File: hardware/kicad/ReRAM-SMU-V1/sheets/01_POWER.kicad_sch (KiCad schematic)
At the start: 1 part

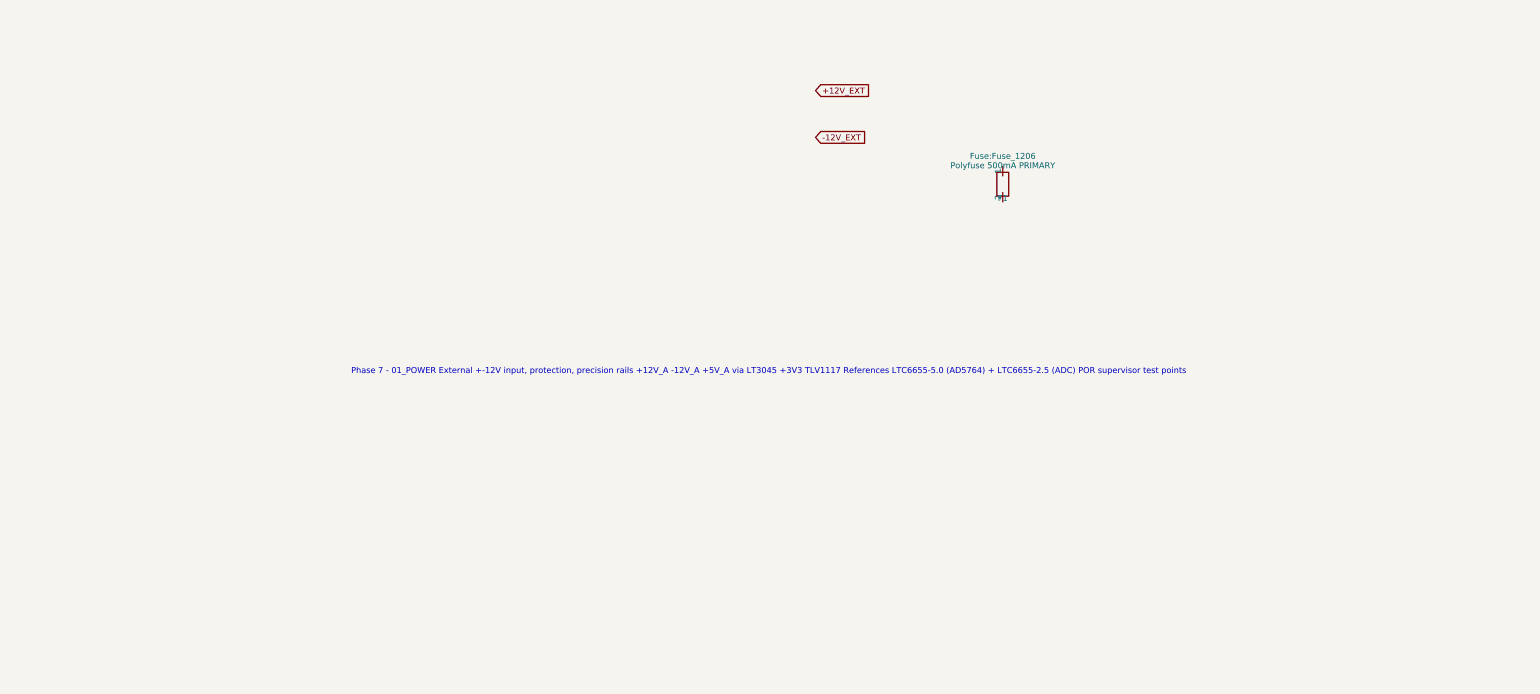
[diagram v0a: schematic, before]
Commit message: hardware: pre-ERC manufacturer corrections (LT1970 physical pins, ADS1262 TSSOP-28, MCU G431RBT6, 74LVC1G74 latch, LT5400 Kelvin, AD5764 rails, ADS1262 bipolar)
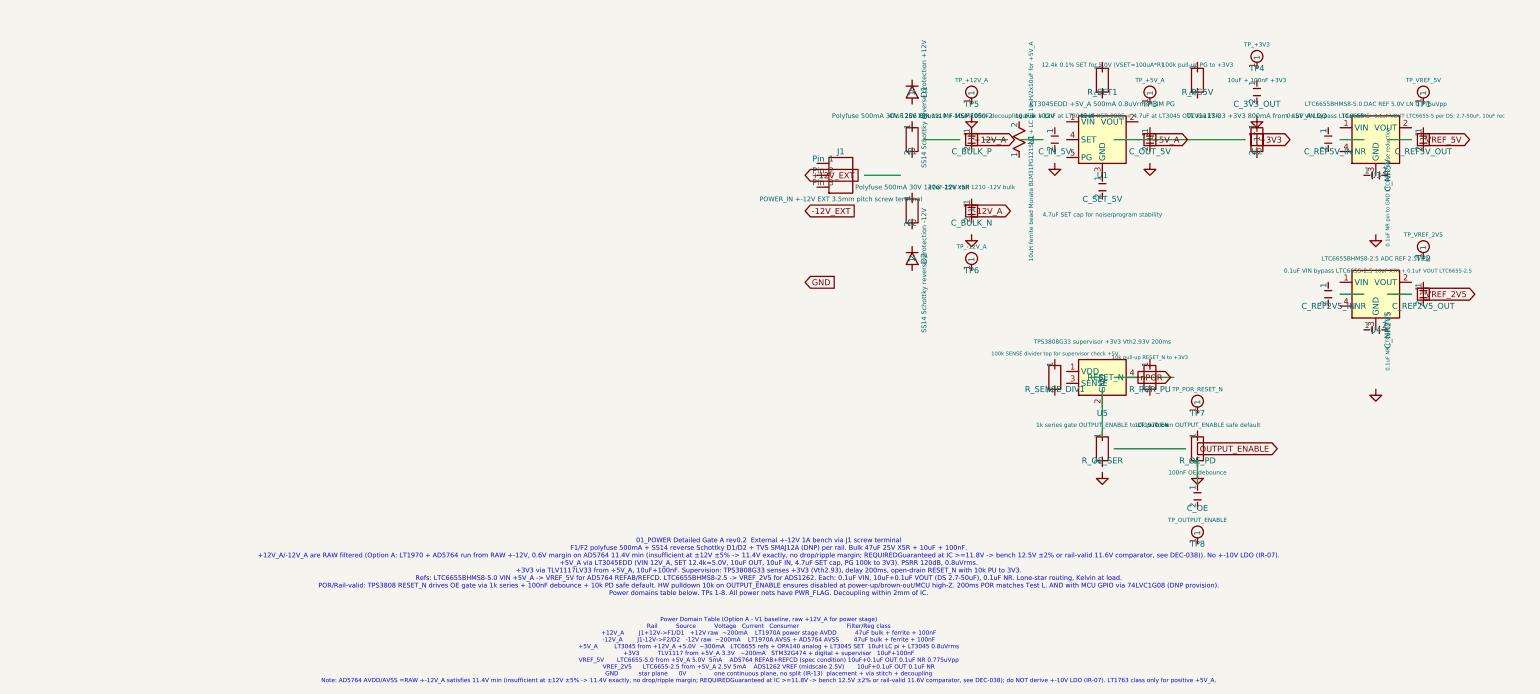
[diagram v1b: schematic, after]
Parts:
- added C_3V3_OUT: 10uF + 100nF +3V3, Capacitor_SMD:C_0805_2012Metric, symbol Device:C
- added C_BULK_N: 47uF 25V X5R 1210 -12V bulk, Capacitor_SMD:C_1210_3225Metric, symbol Device:C
- added C_BULK_P: 47uF 25V X5R 1210 + 10uF 100nF decoupling bulk +1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, Capacitor_SMD:C_1210_3225Metric, symbol Device:C
- added C_IN_5V: 10uF + 100nF at LT3045 IN, Capacitor_SMD:C_0805_2012Metric, symbol Device:C
- added C_NR2V5: 0.1uF NR LTC6655-2.5, Capacitor_SMD:C_0603_1608Metric, symbol Device:C
- added C_NR5V: 0.1uF NR pin to GND LTC6655 noise reduction, Capacitor_SMD:C_0603_1608Metric, symbol Device:C
- added C_OE: 100nF OE debounce, Capacitor_SMD:C_0603_1608Metric, symbol Device:C
- added C_OUT_5V: 10uF X5R 0805 + 4.7uF at LT3045 OUT low ESR, Capacitor_SMD:C_0805_2012Metric, symbol Device:C
- added C_REF2V5_IN: 0.1uF VIN bypass LTC6655-2.5, Capacitor_SMD:C_0603_1608Metric, symbol Device:C
- added C_REF2V5_OUT: 10uF X7R + 0.1uF VOUT LTC6655-2.5, Capacitor_SMD:C_0805_2012Metric, symbol Device:C
- added C_REF5V_IN: 0.1uF VIN bypass LTC6655-5, Capacitor_SMD:C_0603_1608Metric, symbol Device:C
- added C_REF5V_OUT: 10uF X7R + 0.1uF VOUT LTC6655-5 per DS: 2.7-50uF,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, Capacitor_SMD:C_0805_2012Metric, symbol Device:C
- added C_SET_5V: 4.7uF SET cap for noise/program stability, Capacitor_SMD:C_0603_1608Metric, symbol Device:C
- added D1: SS14 Schottky reverse protection +12V, Diode_SMD:D_SMA, symbol Device:D_Schottky
- added D2: SS14 Schottky reverse protection -12V, Diode_SMD:D_SMA, symbol Device:D_Schottky
- added F2: Polyfuse 500mA 30V 1206 -12V rail, Fuse:Fuse_1206_3216Metric, symbol Device:R
- added J1: POWER_IN +-12V EXT 3.5mm pitch screw terminal, Connector_Screw:Connector_Screw_Terminal_3.5mm_3pin, symbol Connector_Generic:Conn_03x01_Odd_Even
- added L1: 10uH ferrite bead Murata BLM31PG121SN1 + LC pi 10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, Inductor_SMD:L_1206_3216Metric, symbol Device:L
- added R_OE_PD: 10k pulldown OUTPUT_ENABLE safe default, Resistor_SMD:R_0603_1608Metric, symbol Device:R
- added R_OE_SER: 1k series gate OUTPUT_ENABLE to LT1970 EN, Resistor_SMD:R_0603_1608Metric, symbol Device:R
- added R_PG5V: 100k pull-up PG to +3V3, Resistor_SMD:R_0603_1608Metric, symbol Device:R
- added R_POR_PU: 10k pull-up RESET_N to +3V3, Resistor_SMD:R_0603_1608Metric, symbol Device:R
- added R_SENSE_DIV1: 100k SENSE divider top for supervisor check +5V, Resistor_SMD:R_0603_1608Metric, symbol Device:R
- added R_SET1: 12.4k 0.1% SET for 5.0V (VSET=100uA*R), Resistor_SMD:R_0603_1608Metric, symbol Device:R
- added TP1: TP_VREF_5V, symbol ReRAM_SMU:TestPoint
- added TP2: TP_VREF_2V5, symbol ReRAM_SMU:TestPoint
- added TP3: TP_+5V_A, symbol ReRAM_SMU:TestPoint
- added TP4: TP_+3V3, symbol ReRAM_SMU:TestPoint
- added TP5: TP_+12V_A, symbol ReRAM_SMU:TestPoint
- added TP6: TP_-12V_A, symbol ReRAM_SMU:TestPoint
- added TP7: TP_POR_RESET_N, symbol ReRAM_SMU:TestPoint
- added TP8: TP_OUTPUT_ENABLE, symbol ReRAM_SMU:TestPoint
- added U1: LT3045EDD +5V_A 500mA 0.8uVrms ILIM PG, Package_DFN:DFN-12_3x3mm_P0.45mm_EP, symbol ReRAM_SMU:LT3045
- added U2: TLV1117-33 +3V3 800mA from +5V_A LDO, Package_TO_SOT_SMD:SOT-223-3_TabPin2, symbol Device:R
- added U3: LTC6655BHMS8-5.0 DAC REF 5.0V LN 0.775uVpp, Package_SO:MSOP-8_3x3mm_P0.65mm, symbol ReRAM_SMU:LTC6655-5
- added U4: LTC6655BHMS8-2.5 ADC REF 2.5V LN, Package_SO:MSOP-8_3x3mm_P0.65mm, symbol ReRAM_SMU:LTC6655-2V5
- added U5: TPS3808G33 supervisor +3V3 Vth2.93V 200ms, Package_TO_SOT_SMD:SOT-23-6, symbol ReRAM_SMU:TPS3808
- F1: value Polyfuse 500mA PRIMARY -> Polyfuse 500mA 30V 1206 Bourns MF-MSMF050-2; footprint Fuse:Fuse_1206 -> Fuse:Fuse_1206_3216Metric
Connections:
- new net: C_SET_5V.1, U1.3 (GND)
- new net nPOR: U5.4 (RESET_N)
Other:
- note added: "01_POWER Detailed Gate A rev0.2 External +-12V 1A bench via J1 screw terminal F1/F2 polyfuse 500mA + SS14 reverse Schottky D1/D2 + TVS SMAJ12A (DNP) per rail. Bulk 47uF 25V X5R + 10uF + 100nF. +12V_A/-12V_A are RAW filtered (Option A: LT1970 + AD5764 run from RAW +-12V, 0.6V margin on AD5764 11.4V min (insufficient at ±12V ±5% -> 11.4V exactly, no drop/ripple margin; REQUIREDGuaranteed at IC >=11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"
- note added: "Power Domain Table (Option A - V1 baseline, raw +12V_A for power stage) Rail Source Voltage Current Consumer Filter/Reg class +12V_A J1+12V->F1/D1 +12V raw ~200mA LT1970A power stage AVDD 47uF bulk + ferrite + 100nF -12V_A J1-12V->F2/D2 -12V raw ~200mA LT1970A AVSS + AD5764 AVSS 47uF bulk + ferrite + 100nF +5V_A LT3045 from +12V_A +5.0V ~300mA LTC6655 refs + OPA140 analog + LT3045 SET 10uH LC pi 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"
- note removed: "Phase 7 - 01_POWER External +-12V input, protection, precision rails +12V_A -12V_A +5V_A via LT3045 +3V3 TLV1117 References LTC6655-5.0 (AD5764) + LTC6655-2.5 (ADC) POR supervisor test points"

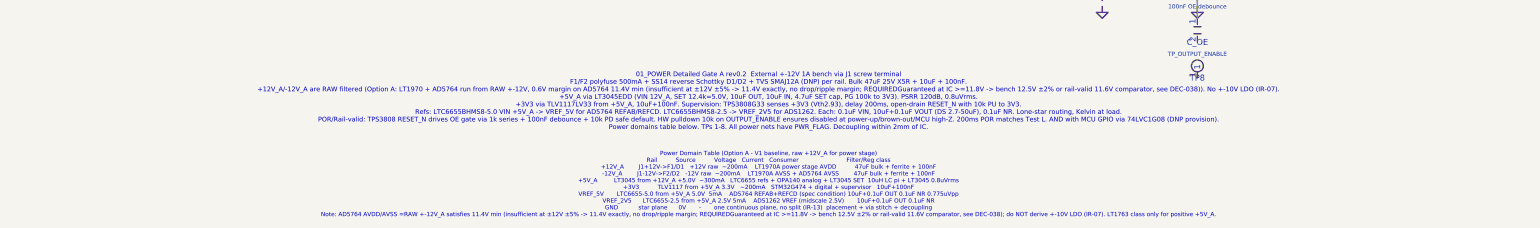
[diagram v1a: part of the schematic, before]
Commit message: hardware: pre-ERC correction gate 2 (LT1970 consistency, LT5400A-1 MSOP-8, ADS1262IPW 28-pin, bipolar ±2.5V, buffer per-range, power baseline normalize)
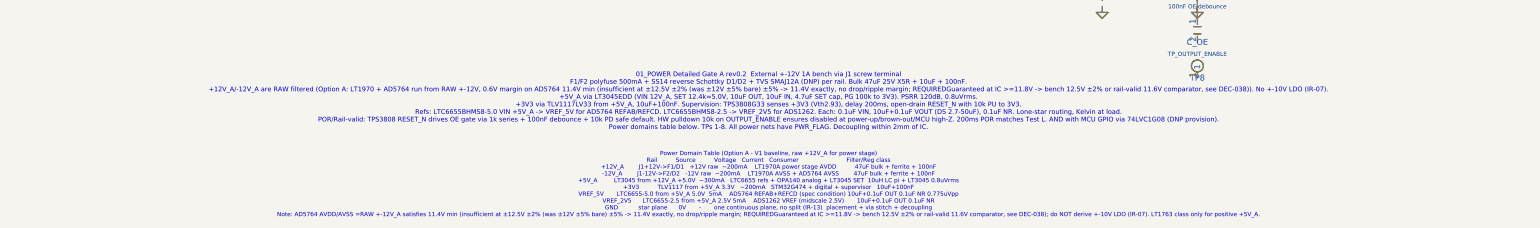
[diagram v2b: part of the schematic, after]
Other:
- note added: "01_POWER Detailed Gate A rev0.2 External +-12V 1A bench via J1 screw terminal F1/F2 polyfuse 500mA + SS14 reverse Schottky D1/D2 + TVS SMAJ12A (DNP) per rail. Bulk 47uF 25V X5R + 10uF + 100nF. +12V_A/-12V_A are RAW filtered (Option A: LT1970 + AD5764 run from RAW +-12V, 0.6V margin on AD5764 11.4V min (insufficient at ±12.5V ±2% (was ±12V ±5% bare) ±5% -> 11.4V exactly, no drop/ripple margin; REQ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"
- note removed: "01_POWER Detailed Gate A rev0.2 External +-12V 1A bench via J1 screw terminal F1/F2 polyfuse 500mA + SS14 reverse Schottky D1/D2 + TVS SMAJ12A (DNP) per rail. Bulk 47uF 25V X5R + 10uF + 100nF. +12V_A/-12V_A are RAW filtered (Option A: LT1970 + AD5764 run from RAW +-12V, 0.6V margin on AD5764 11.4V min (insufficient at ±12V ±5% -> 11.4V exactly, no drop/ripple margin; REQUIREDGuaranteed at IC >=11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"
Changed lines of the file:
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@@
 	(global_label "OUTPUT_ENABLE" (shape output) (at 101.6 96.52 0) (effects (font (size 1.27 1.27))))
 	(global_label "nPOR" (shape output) (at 88.9 81.28 0) (effects (font (size 1.27 1.27))))
-	(text "01_POWER Detailed Gate A rev0.2  External +-12V 1A bench via J1 screw terminal\nF1/F2 polyfuse 500mA + SS14 reverse Schottky D1/D2 + TVS SMAJ12A (DNP) per rail. Bulk 47uF 25V X5R + 10uF + 100nF.\n+12V_A/-12V_A are RAW filtered (Option A: LT1970 + AD5764 run from RAW +-12V, 0.6V margin on AD5764 11.4V min (insufficient at ±12V ±5% -> 11.4V exactly, no drop/ripple margin; REQUIREDGuaranteed at IC >=11.8V -> bench 12.5V ±2% or rail-valid 11.6V comparator, see DEC-038)). No +-10V LDO (IR-07).\n+5V_A via LT3045EDD (VIN 12V_A, SET 12.4k=5.0V, 10uF OUT, 10uF IN, 4.7uF SET cap, PG 100k to 3V3). PSRR 120dB, 0.8uVrms.\n+3V3 via TLV1117LV33 from +5V_A, 10uF+100nF. Supervision: TPS3808G33 senses +3V3 (Vth2.93), delay 200ms, open-drain RESET_N with 10k PU to 3V3.\nRefs: LTC6655BHMS8-5.0 VIN +5V_A -> VREF_5V for AD5764 REFAB/REFCD. LTC6655BHMS8-2.5 -> VREF_2V5 for ADS1262. Each: 0.1uF VIN, 10uF+0.1uF VOUT (DS 2.7-50uF), 0.1uF NR. Lone-star routing, Kelvin at load.\nPOR/Rail-valid: TPS3808 RESET_N drives OE gate via 1k series + 100nF debounce + 10k PD safe default. HW pulldown 10k on OUTPUT_ENABLE ensures disabled at power-up/brown-out/MCU high-Z. 200ms POR matches Test L. AND with MCU GPIO via 74LVC1G08 (DNP provision).\nPower domains table below. TPs 1-8. All power nets have PWR_FLAG. Decoupling within 2mm of IC." (at 10 121.92 0) (effects (font (size 1 1))))
-	(text "Power Domain Table (Option A - V1 baseline, raw +12V_A for power stage)\nRail          Source          Voltage   Current   Consumer                          Filter/Reg class\n+12V_A        J1+12V->F1/D1   +12V raw  ~200mA    LT1970A power stage AVDD          47uF bulk + ferrite + 100nF\n-12V_A        J1-12V->F2/D2   -12V raw  ~200mA    LT1970A AVSS + AD5764 AVSS        47uF bulk + ferrite + 100nF\n+5V_A         LT3045 from +12V_A +5.0V  ~300mA   LTC6655 refs + OPA140 analog + LT3045 SET  10uH LC pi + LT3045 0.8uVrms\n+3V3          TLV1117 from +5V_A 3.3V   ~200mA   STM32G474 + digital + supervisor   10uF+100nF\nVREF_5V       LTC6655-5.0 from +5V_A 5.0V  5mA    AD5764 REFAB+REFCD (spec condition) 10uF+0.1uF OUT 0.1uF NR 0.775uVpp\nVREF_2V5      LTC6655-2.5 from +5V_A 2.5V 5mA    ADS1262 VREF (midscale 2.5V)       10uF+0.1uF OUT 0.1uF NR\nGND           star plane      0V       -       one continuous plane, no split (IR-13)  placement + via stitch + decoupling\nNote: AD5764 AVDD/AVSS =RAW +-12V_A satisfies 11.4V min (insufficient at ±12V ±5% -> 11.4V exactly, no drop/ripple margin; REQUIREDGuaranteed at IC >=11.8V -> bench 12.5V ±2% or rail-valid 11.6V comparator, see DEC-038); do NOT derive +-10V LDO (IR-07). LT1763 class only for positive +5V_A." (at 10 139.7 0) (effects (font (size 0.9 0.9))))
+	(text "01_POWER Detailed Gate A rev0.2  External +-12V 1A bench via J1 screw terminal\nF1/F2 polyfuse 500mA + SS14 reverse Schottky D1/D2 + TVS SMAJ12A (DNP) per rail. Bulk 47uF 25V X5R + 10uF + 100nF.\n+12V_A/-12V_A are RAW filtered (Option A: LT1970 + AD5764 run from RAW +-12V, 0.6V margin on AD5764 11.4V min (insufficient at ±12.5V ±2% (was ±12V ±5% bare) ±5% -> 11.4V exactly, no drop/ripple margin; REQUIREDGuaranteed at IC >=11.8V -> bench 12.5V ±2% or rail-valid 11.6V comparator, see DEC-038)). No +-10V LDO (IR-07).\n+5V_A via LT3045EDD (VIN 12V_A, SET 12.4k=5.0V, 10uF OUT, 10uF IN, 4.7uF SET cap, PG 100k to 3V3). PSRR 120dB, 0.8uVrms.\n+3V3 via TLV1117LV33 from +5V_A, 10uF+100nF. Supervision: TPS3808G33 senses +3V3 (Vth2.93), delay 200ms, open-drain RESET_N with 10k PU to 3V3.\nRefs: LTC6655BHMS8-5.0 VIN +5V_A -> VREF_5V for AD5764 REFAB/REFCD. LTC6655BHMS8-2.5 -> VREF_2V5 for ADS1262. Each: 0.1uF VIN, 10uF+0.1uF VOUT (DS 2.7-50uF), 0.1uF NR. Lone-star routing, Kelvin at load.\nPOR/Rail-valid: TPS3808 RESET_N drives OE gate via 1k series + 100nF debounce + 10k PD safe default. HW pulldown 10k on OUTPUT_ENABLE ensures disabled at power-up/brown-out/MCU high-Z. 200ms POR matches Test L. AND with MCU GPIO via 74LVC1G08 (DNP provision).\nPower domains table below. TPs 1-8. All power nets have PWR_FLAG. Decoupling within 2mm of IC." (at 10 121.92 0) (effects (font (size 1 1))))
+	(text "Power Domain Table (Option A - V1 baseline, raw +12V_A for power stage)\nRail          Source          Voltage   Current   Consumer                          Filter/Reg class\n+12V_A        J1+12V->F1/D1   +12V raw  ~200mA    LT1970A power stage AVDD          47uF bulk + ferrite + 100nF\n-12V_A        J1-12V->F2/D2   -12V raw  ~200mA    LT1970A AVSS + AD5764 AVSS        47uF bulk + ferrite + 100nF\n+5V_A         LT3045 from +12V_A +5.0V  ~300mA   LTC6655 refs + OPA140 analog + LT3045 SET  10uH LC pi + LT3045 0.8uVrms\n+3V3          TLV1117 from +5V_A 3.3V   ~200mA   STM32G474 + digital + supervisor   10uF+100nF\nVREF_5V       LTC6655-5.0 from +5V_A 5.0V  5mA    AD5764 REFAB+REFCD (spec condition) 10uF+0.1uF OUT 0.1uF NR 0.775uVpp\nVREF_2V5      LTC6655-2.5 from +5V_A 2.5V 5mA    ADS1262 VREF (midscale 2.5V)       10uF+0.1uF OUT 0.1uF NR\nGND           star plane      0V       -       one continuous plane, no split (IR-13)  placement + via stitch + decoupling\nNote: AD5764 AVDD/AVSS =RAW +-12V_A satisfies 11.4V min (insufficient at ±12.5V ±2% (was ±12V ±5% bare) ±5% -> 11.4V exactly, no drop/ripple margin; REQUIREDGuaranteed at IC >=11.8V -> bench 12.5V ±2% or rail-valid 11.6V comparator, see DEC-038); do NOT derive +-10V LDO (IR-07). LT1763 class only for positive +5V_A." (at 10 139.7 0) (effects (font (size 0.9 0.9))))
 )

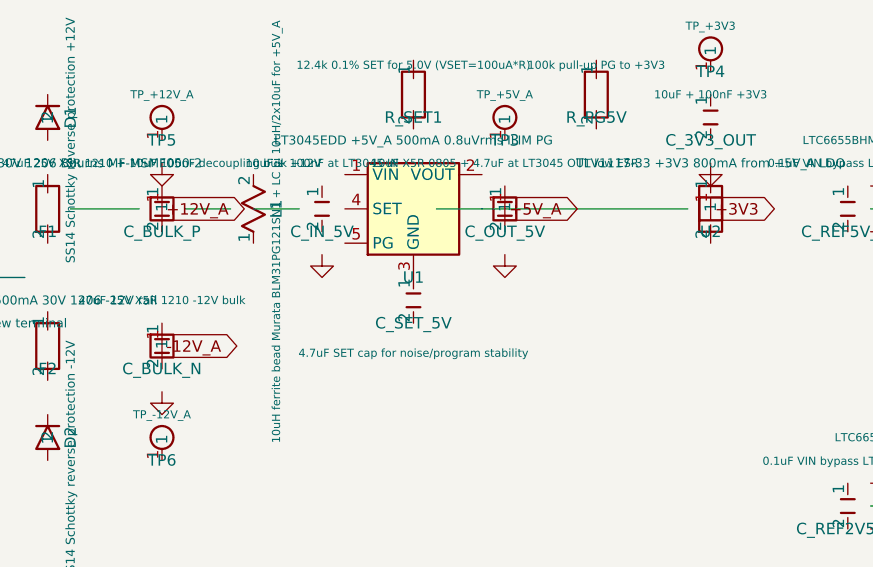
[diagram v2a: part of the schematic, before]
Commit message: hardware: point-to-point wiring progress (01 POWER PWR_FLAG, 02 AD5764 supplies, NC markers) — ERC 439 errors, wiring continues
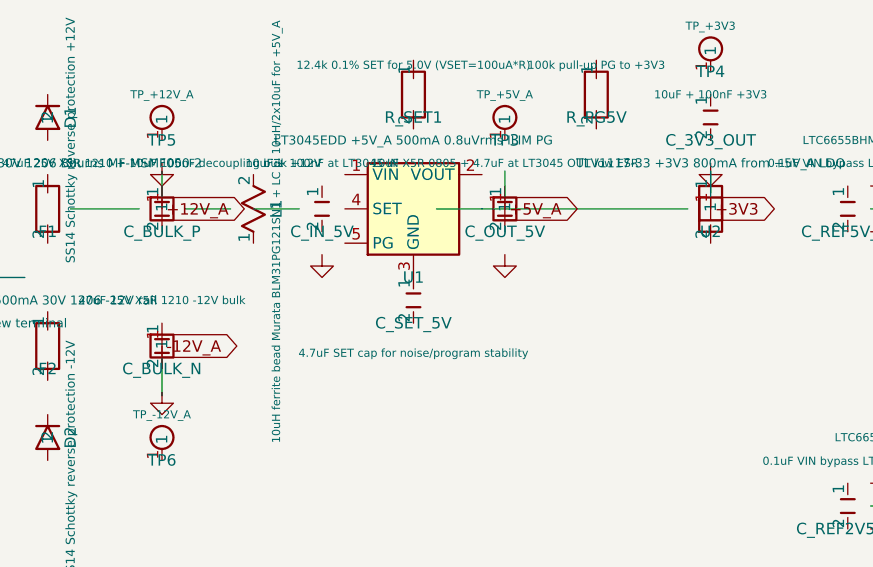
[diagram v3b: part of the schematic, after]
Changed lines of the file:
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@@
 	(text "01_POWER Detailed Gate A rev0.2  External +-12V 1A bench via J1 screw terminal\nF1/F2 polyfuse 500mA + SS14 reverse Schottky D1/D2 + TVS SMAJ12A (DNP) per rail. Bulk 47uF 25V X5R + 10uF + 100nF.\n+12V_A/-12V_A are RAW filtered (Option A: LT1970 + AD5764 run from RAW +-12V, 0.6V margin on AD5764 11.4V min (insufficient at ±12.5V ±2% (was ±12V ±5% bare) ±5% -> 11.4V exactly, no drop/ripple margin; REQUIREDGuaranteed at IC >=11.8V -> bench 12.5V ±2% or rail-valid 11.6V comparator, see DEC-038)). No +-10V LDO (IR-07).\n+5V_A via LT3045EDD (VIN 12V_A, SET 12.4k=5.0V, 10uF OUT, 10uF IN, 4.7uF SET cap, PG 100k to 3V3). PSRR 120dB, 0.8uVrms.\n+3V3 via TLV1117LV33 from +5V_A, 10uF+100nF. Supervision: TPS3808G33 senses +3V3 (Vth2.93), delay 200ms, open-drain RESET_N with 10k PU to 3V3.\nRefs: LTC6655BHMS8-5.0 VIN +5V_A -> VREF_5V for AD5764 REFAB/REFCD. LTC6655BHMS8-2.5 -> VREF_2V5 for ADS1262. Each: 0.1uF VIN, 10uF+0.1uF VOUT (DS 2.7-50uF), 0.1uF NR. Lone-star routing, Kelvin at load.\nPOR/Rail-valid: TPS3808 RESET_N drives OE gate via 1k series + 100nF debounce + 10k PD safe default. HW pulldown 10k on OUTPUT_ENABLE ensures disabled at power-up/brown-out/MCU high-Z. 200ms POR matches Test L. AND with MCU GPIO via 74LVC1G08 (DNP provision).\nPower domains table below. TPs 1-8. All power nets have PWR_FLAG. Decoupling within 2mm of IC." (at 10 121.92 0) (effects (font (size 1 1))))
 	(text "Power Domain Table (Option A - V1 baseline, raw +12V_A for power stage)\nRail          Source          Voltage   Current   Consumer                          Filter/Reg class\n+12V_A        J1+12V->F1/D1   +12V raw  ~200mA    LT1970A power stage AVDD          47uF bulk + ferrite + 100nF\n-12V_A        J1-12V->F2/D2   -12V raw  ~200mA    LT1970A AVSS + AD5764 AVSS        47uF bulk + ferrite + 100nF\n+5V_A         LT3045 from +12V_A +5.0V  ~300mA   LTC6655 refs + OPA140 analog + LT3045 SET  10uH LC pi + LT3045 0.8uVrms\n+3V3          TLV1117 from +5V_A 3.3V   ~200mA   STM32G474 + digital + supervisor   10uF+100nF\nVREF_5V       LTC6655-5.0 from +5V_A 5.0V  5mA    AD5764 REFAB+REFCD (spec condition) 10uF+0.1uF OUT 0.1uF NR 0.775uVpp\nVREF_2V5      LTC6655-2.5 from +5V_A 2.5V 5mA    ADS1262 VREF (midscale 2.5V)       10uF+0.1uF OUT 0.1uF NR\nGND           star plane      0V       -       one continuous plane, no split (IR-13)  placement + via stitch + decoupling\nNote: AD5764 AVDD/AVSS =RAW +-12V_A satisfies 11.4V min (insufficient at ±12.5V ±2% (was ±12V ±5% bare) ±5% -> 11.4V exactly, no drop/ripple margin; REQUIREDGuaranteed at IC >=11.8V -> bench 12.5V ±2% or rail-valid 11.6V comparator, see DEC-038); do NOT derive +-10V LDO (IR-07). LT1763 class only for positive +5V_A." (at 10 139.7 0) (effects (font (size 0.9 0.9))))
+	(wire (pts (xy 53.34 26.27) (xy 53.34 30.48)) (stroke (width 0) (type default)) (uuid "wire-pwr-correct-53.34-25"))
+	(wire (pts (xy 53.34 51.27) (xy 53.34 45.72)) (stroke (width 0) (type default)) (uuid "wire-pwr-correct-53.34-50"))
+	(wire (pts (xy 91.44 26.27) (xy 91.44 30.48)) (stroke (width 0) (type default)) (uuid "wire-pwr-correct-91.44-25"))
+	(wire (pts (xy 114.3 26.27) (xy 114.3 30.48)) (stroke (width 0) (type default)) (uuid "wire-pwr-correct-114.3-25"))
 )
